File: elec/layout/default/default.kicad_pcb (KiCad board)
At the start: 2 copper layers, 71.5 x 75.5 mm, 25 parts

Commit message: Prune dead vendored code; gitignore generated passive parts
Remove ~188 files of unused vendored sources that the build never touches
(verified via import-closure from bedpresence.ato + referenced footprint
assets; rebuild + DRC confirm the board is byte-for-byte behaviour-identical,
0 unconnected):

- esp32c3-ato/ (alternative ESP32-C3 micro, unused)
- esp32-s3/ sub-projects: bq24045dsqr, tps63020dsjr, sk6805-ec20, tf-01a,
  and nested usb-connectors/programming-headers copies
- generics/ modules the design doesn't use (resistors, capacitors, diodes,
  mosfets, opamps, oscillators, leds, filters, ... + their 3dshapes)
- duplicate footprints.3dshapes / mech / metadata / .github dirs
- three orphan top-level .ato files

Gitignore the four picker-generated passive part dirs (Samsung caps,
UNI_ROYAL resistors, ~21MB of 3D models): atopile regenerates them from the
Capacitor/Resistor constraints on every build, so they're cache, not source.

elec/src: 46M -> ~4M tracked.

Co-Authored-By: Claude Opus 4.8 <noreply@anthropic.com>
Claude-Session: https://claude.ai/code/session_01CzFBP36YaBDQ7hT4gCErw4
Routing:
- net lv: track 15.8 -> 24.8 mm, vias 9 -> 10
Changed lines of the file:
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@@
+	)
+	(via
+		(at 145 86.5)
+		(size 0.6)
+		(drill 0.3)
+		(layers "F.Cu" "B.Cu")
+		(net 6)
+		(free yes)
 	)
 	(via
@@
 		(net 6)
 	)
+	(segment
+		(start 121.25 90.5)
+		(end 121 90.5)
+		(width 0.2)
+		(layer "B.Cu")
+		(net 6)
+	)
+	(segment
+		(start 124 87.75)
+		(end 121.25 90.5)
+		(width 0.2)
+		(layer "B.Cu")
+		(net 6)
+	)
+	(segment
+		(start 127.25 91)
+		(end 124 87.75)
+		(width 0.2)
+		(layer "B.Cu")
+		(net 6)
+	)
+	(segment
+		(start 127.25 91)
+		(end 127.5 91)
+		(width 0.2)
+		(layer "B.Cu")
+		(net 6)
+	)

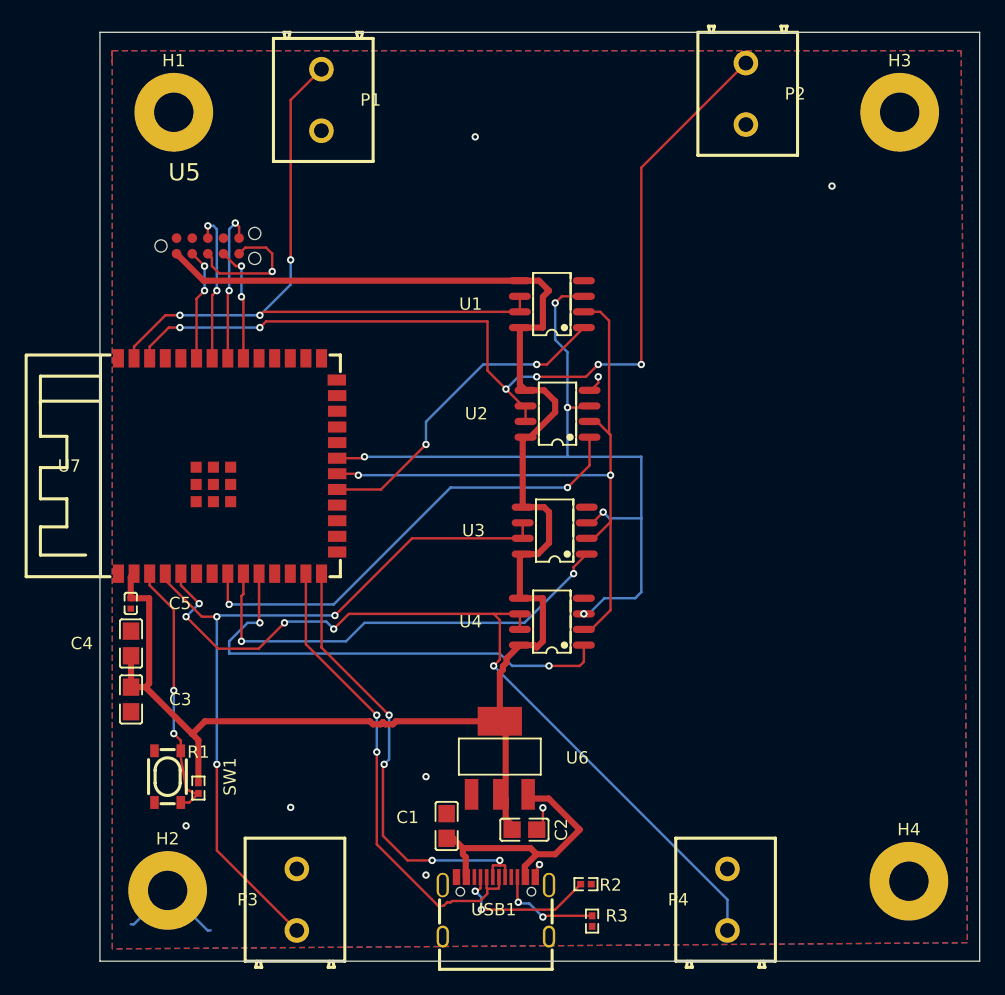
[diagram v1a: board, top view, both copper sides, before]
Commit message: Apply design-review fixes; finish routing and antenna keepout
Review fixes in ato source:
- 100nF decoupling on each MCP41010 digipot
- 3.9k series resistors capping digipot wiper current below the 1mA
  abs max even with the FSR fully pressed
- 1k + 100nF RC filters between sense nodes and the ESP32 ADC pins
- 1uF EN cap for power-on-reset delay per Espressif guidelines
- CC resistors tightened to 5.1k +/-5% (picker chose 4.7k at +/-20%)
- AMS1117 output cap bumped to 22uF per datasheet stability note

Layout: placed the new parts, restored the ground zone net after the
rebuild dropped it, fixed stranded ground islands and starved thermal
reliefs, added the antenna copper keepout under the WROOM overhang.
DRC is clean (0 errors, cosmetic silk warnings only) and JLCPCB DFM
checks pass.

Co-Authored-By: Claude Fable 5 <noreply@anthropic.com>
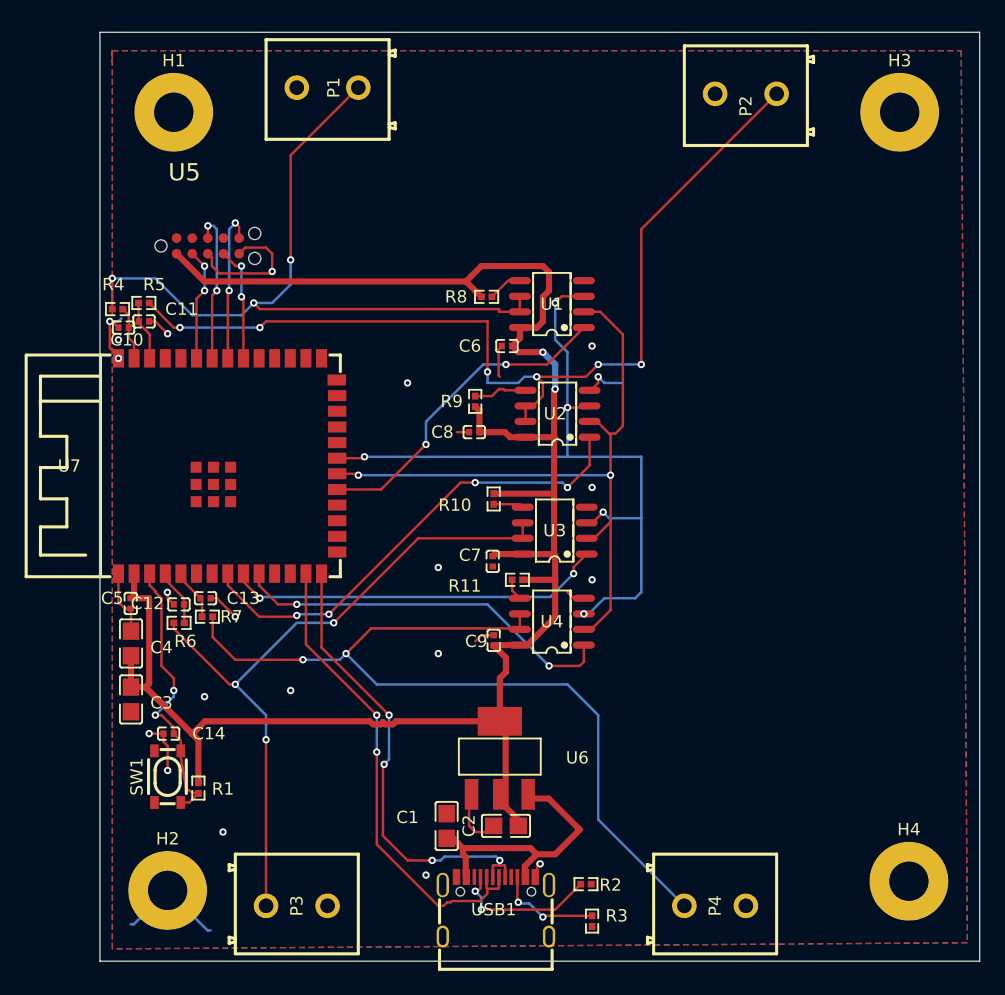
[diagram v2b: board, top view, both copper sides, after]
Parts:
- added C10: 100nF ±10%, Samsung_Electro_Mechanics_CL05B104KO5NNNC:C0402, F.Cu at (120.4, 42.0)
- added C11: 100nF ±10%, Samsung_Electro_Mechanics_CL05B104KO5NNNC:C0402, F.Cu at (122.1, 41.5)
- added C12: 100nF ±10%, Samsung_Electro_Mechanics_CL05B104KO5NNNC:C0402, F.Cu at (124.9, 64.5)
- added C13: 100nF ±10%, Samsung_Electro_Mechanics_CL05B104KO5NNNC:C0402, F.Cu at (127.1, 64.0)
- added C14: 1µF ±10%, Samsung_Electro_Mechanics_CL05A105KA5NQNC:C0402, F.Cu at (124.1, 75.0)
- added C6: 100nF ±10%, Samsung_Electro_Mechanics_CL05B104KO5NNNC:C0402, F.Cu at (151.6, 43.5)
- added C7: 100nF ±10%, Samsung_Electro_Mechanics_CL05B104KO5NNNC:C0402, F.Cu at (150.4, 61.0)
- added C8: 100nF ±10%, Samsung_Electro_Mechanics_CL05B104KO5NNNC:C0402, F.Cu at (148.9, 50.5)
- added C9: 100nF ±10%, Samsung_Electro_Mechanics_CL05B104KO5NNNC:C0402, F.Cu at (150.5, 67.4)
- added R10: 4.02kΩ ±1%, UNI_ROYAL_0402WGF4021TCE:R0402, F.Cu at (150.5, 55.9)
- added R11: 4.02kΩ ±1%, UNI_ROYAL_0402WGF4021TCE:R0402, F.Cu at (152.4, 62.5)
- added R4: 1kΩ ±1%, UNI_ROYAL_0402WGF1001TCE:R0402, F.Cu at (119.9, 40.5)
- added R5: 1kΩ ±1%, UNI_ROYAL_0402WGF1001TCE:R0402, F.Cu at (122.1, 40.0)
- added R6: 1kΩ ±1%, UNI_ROYAL_0402WGF1001TCE:R0402, F.Cu at (124.9, 66.0)
- added R7: 1kΩ ±1%, UNI_ROYAL_0402WGF1001TCE:R0402, F.Cu at (127.2, 65.5)
- added R8: 4.02kΩ ±1%, UNI_ROYAL_0402WGF4021TCE:R0402, F.Cu at (149.9, 39.5)
- added R9: 4.02kΩ ±1%, UNI_ROYAL_0402WGF4021TCE:R0402, F.Cu at (149.0, 48.0)
- C2: value 10µF ±10% -> 22µF ±20%; footprint Samsung_Electro_Mechanics_CL21A106KAYNNNE:C0805 -> Samsung_Electro_Mechanics_CL21A226MAQNNNE:C0805
- R2, R3: value 4.7kΩ ±1% -> 5.1kΩ ±1%; footprint UNI_ROYAL_0402WGF4701TCE:R0402 -> UNI_ROYAL_0402WGF5101TCE:R0402
- moved C2 1.53 mm to (151.5, 82.5), turned to 180 degrees
- moved P1 1.12 mm to (137.0, 22.5), turned to 180 degrees
- moved P4 1.12 mm to (168.5, 89.0), turned to 0 degrees
- moved P3 0.50 mm to (134.5, 89.0), turned to 0 degrees
- turned P2 to 180 degrees
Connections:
- net EN renamed en_cap-power-hv
- U1 pad 5: hv -> 5
- U2 pad 5: hv -> 5-1
- U3 pad 5: hv -> 5-2
- U4 pad 5: hv -> 5-3
- U7 pad 38: 1-1 -> filter_cap2-power-hv
- U7 pad 39: 1 -> filter_cap1-power-hv
- U7 pad 4: 1-2 -> filter_cap3-power-hv
- U7 pad 5: 1-3 -> filter_cap4-power-hv
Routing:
- net lv: track 24.8 -> 57.2 mm, vias 10 -> 20
- net hv: track 140.1 -> 161.0 mm, vias 0 -> 2
- net digi_pot4-spi-cs: track 38.9 -> 31.6 mm
- net 1-2: track 62.4 -> 55.9 mm
- net digi_pot3-spi-cs: track 36.9 -> 30.9 mm
- net filter_cap2-power-hv: track 0.00 -> 4.68 mm
- net filter_cap1-power-hv: track 0.00 -> 4.38 mm
- net 5-1: track 0.00 -> 4.37 mm
- net filter_cap3-power-hv: track 0.00 -> 4.11 mm
- net 1: track 56.8 -> 60.9 mm
- net filter_cap4-power-hv: track 0.00 -> 3.59 mm
- net 5: track 0.00 -> 2.81 mm
- net 5-2: track 0.00 -> 2.46 mm
- net 5-3: track 0.00 -> 1.76 mm
- net en_cap-power-hv: track 17.2 -> 18.7 mm
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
